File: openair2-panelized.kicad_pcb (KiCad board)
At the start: 2 copper layers, 175 x 96 mm, 423 parts, among them IC2 FT231XQ, IC3 SC189Z, IC5 SI7006-A20, IC6 RFM95W, P1 PM, P2 MOD1, P3 MOD2, P4 FAN, P5 PWR, T2 MMBT2222ALT3G, T3 MMBT2222ALT3G, U1 MIC2004-1.2YM5

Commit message: added link to proper tag
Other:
- board text added: "https://github.com/OpenAirCgn/openairnode-hw/tree/cgn-noise-i2s"
- board text removed: "https://github.com/OpenAirCgn/openairnode-hw"
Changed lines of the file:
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@@
     (effects (font (size 3 3) (thickness 0.6)) (justify left))
   )
-  (gr_text https://github.com/OpenAirCgn/openairnode-hw (at 47.1 127.9) (layer F.Cu)
-    (effects (font (size 3 3) (thickness 0.6)) (justify left))
+  (gr_text https://github.com/OpenAirCgn/openairnode-hw/tree/cgn-noise-i2s (at 47.1 127.9) (layer F.Cu)
+    (effects (font (size 1.5 1.5) (thickness 0.3)) (justify left))
   )
   (gr_text JLCJLCJLCJLC (at 206.9 55.2 90) (layer F.Cu)

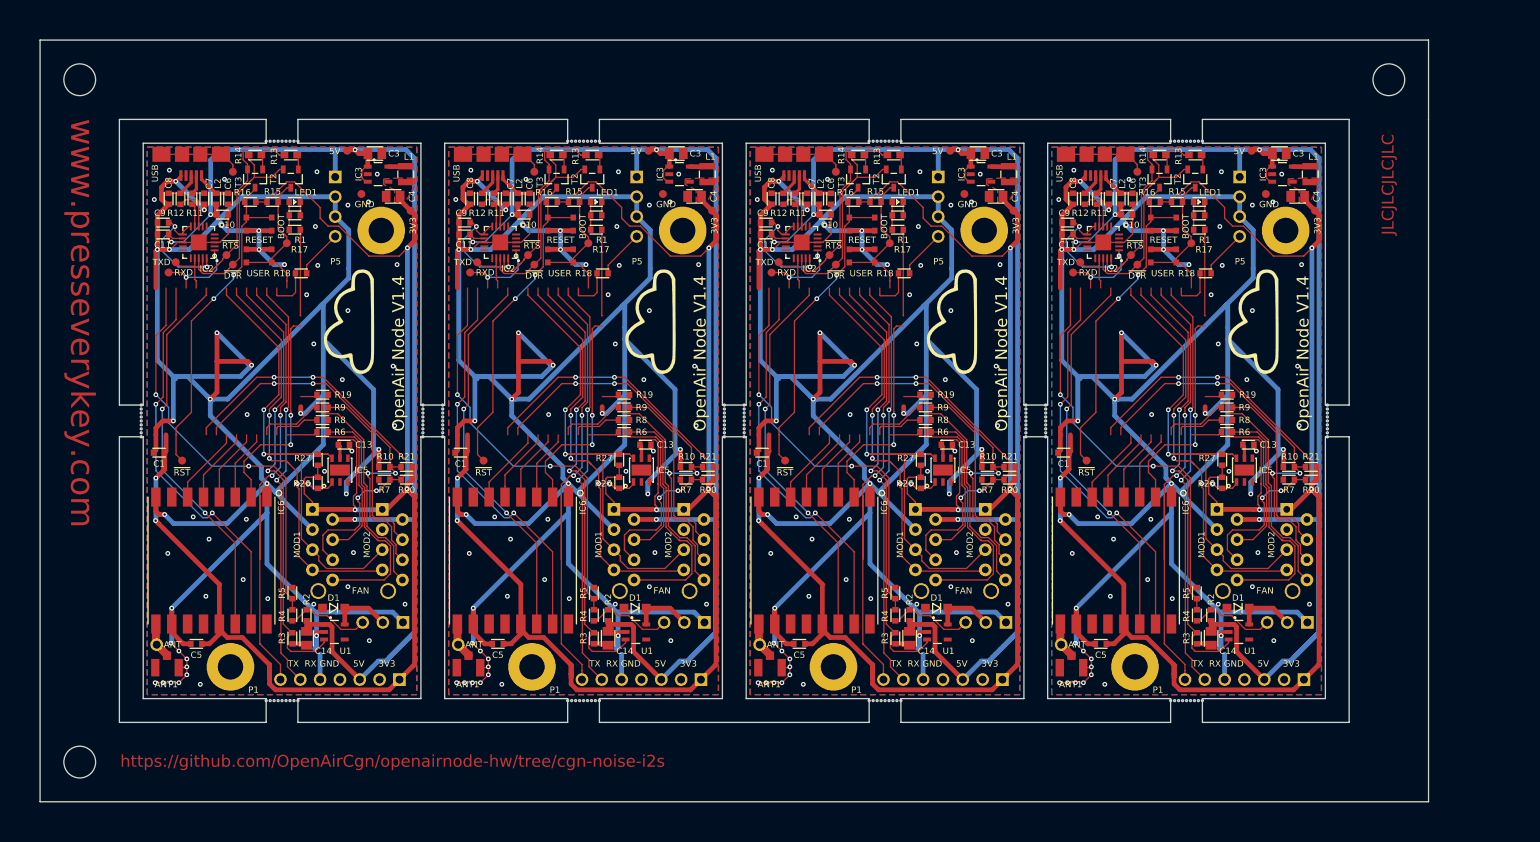
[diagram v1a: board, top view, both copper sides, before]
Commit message: more room for antenna overhang
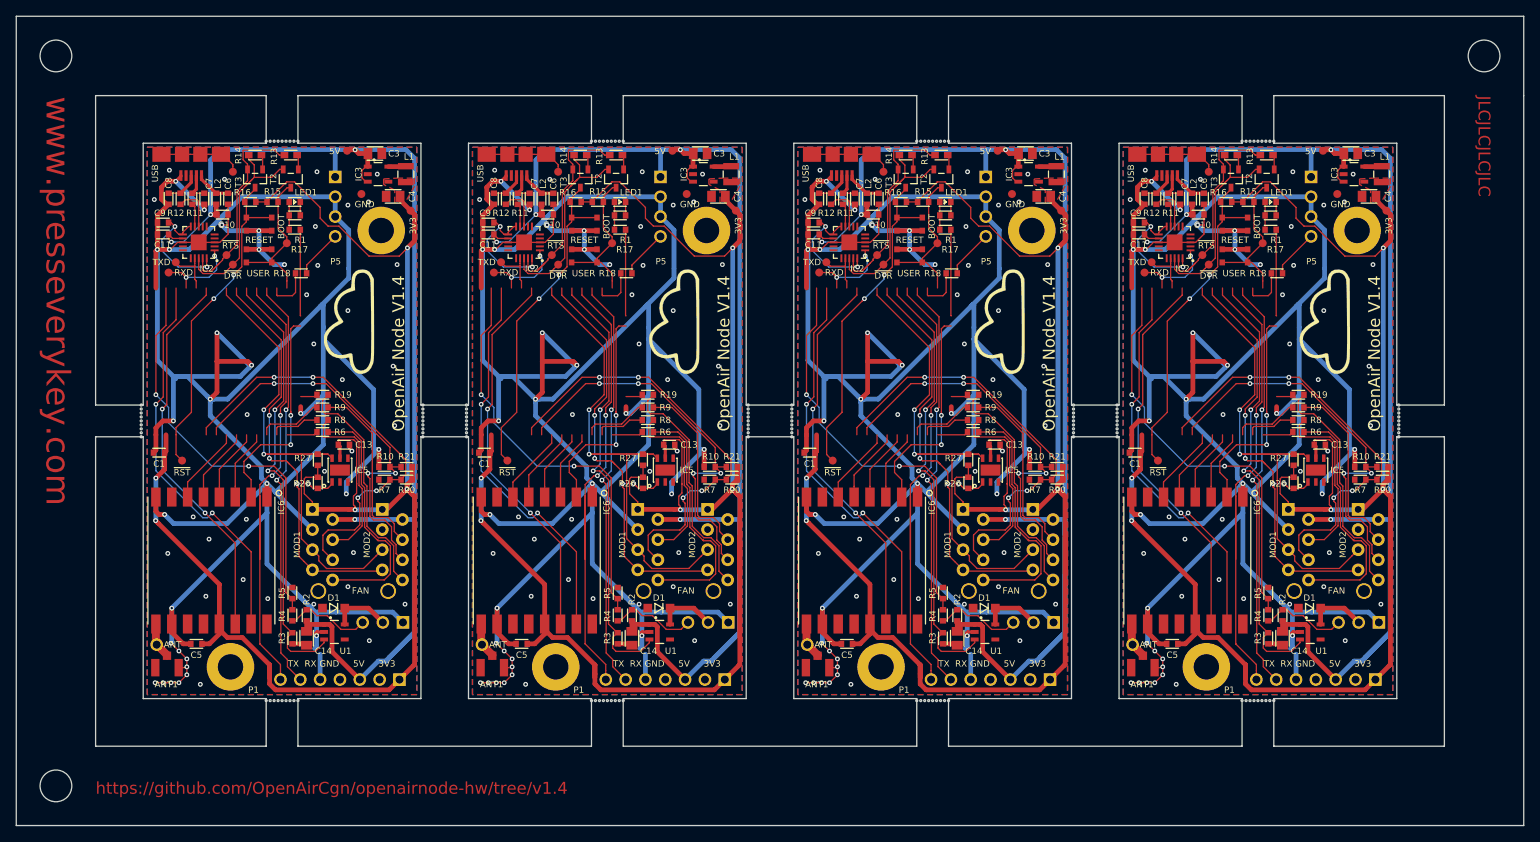
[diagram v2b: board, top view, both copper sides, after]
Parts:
- removed the ANT1 at (167.0, 116.1)
- removed the ANT1 at (129.0, 116.1)
- removed the ANT1 at (91.0, 116.1)
- removed the BTN1 at (178.6, 60.2)
- removed the BTN1 at (140.6, 60.2)
- removed the BTN1 at (102.6, 60.2)
- removed the C1 at (166.0, 89.0)
- removed the C1 at (128.0, 89.0)
- removed the C1 at (90.0, 89.0)
- removed the C10 at (174.0, 59.0)
- removed the C10 at (136.0, 59.0)
- removed the C10 at (98.0, 59.0)
- removed the C11 at (166.5, 61.5)
- removed the C11 at (128.5, 61.5)
- removed the C11 at (90.5, 61.5)
- removed the C13 at (189.3, 88.0)
- removed the C13 at (151.3, 88.0)
- removed the C13 at (113.3, 88.0)
- removed the C13 at (75.3, 88.0)
- removed the C14 at (184.6, 112.4)
- removed the C14 at (146.6, 112.4)
- removed the C14 at (108.6, 112.4)
- removed the C3 at (193.2, 51.3)
- removed the C3 at (155.2, 51.3)
- removed the C3 at (117.2, 51.3)
- removed the C4 at (195.5, 56.7)
- removed the C4 at (157.5, 56.7)
- removed the C4 at (119.5, 56.7)
- removed the C5 at (170.7, 113.1)
- removed the C5 at (132.7, 113.1)
- removed the C5 at (94.7, 113.1)
- removed the C5 at (56.7, 113.1)
- removed the C6 at (174.7, 57.0)
- removed the C6 at (136.7, 57.0)
- removed the C6 at (98.7, 57.0)
- removed the C7 at (171.7, 57.0)
- removed the C7 at (133.7, 57.0)
- removed the C7 at (95.7, 57.0)
- removed the C8 at (167.2, 57.0)
- removed the C8 at (129.2, 57.0)
- removed the C8 at (91.2, 57.0)
- removed the C9 at (166.5, 60.0)
- removed the C9 at (128.5, 60.0)
- removed the C9 at (90.5, 60.0)
- removed the C9 at (52.5, 60.0)
- removed the D1 at (188.0, 108.6)
- removed the D1 at (150.0, 108.6)
- removed the D1 at (112.0, 108.6)
- removed the H1 at (175.0, 116.0)
- removed the H1 at (137.0, 116.0)
- removed the H1 at (99.0, 116.0)
- removed the H2 at (194.0, 61.0)
- removed the H2 at (156.0, 61.0)
- removed the H2 at (118.0, 61.0)
- removed the IC2 at (171.0, 62.5)
- removed the IC2 at (133.0, 62.5)
- removed the IC2 at (95.0, 62.5)
- removed the IC2 at (57.0, 62.5)
- removed the IC3 at (193.6, 53.9)
- removed the IC3 at (155.6, 53.9)
- removed the IC3 at (117.6, 53.9)
- removed the IC5 at (188.8, 91.2)
- removed the IC5 at (150.8, 91.2)
- removed the IC5 at (112.8, 91.2)
- removed the IC6 at (172.6, 102.6)
- removed the IC6 at (134.6, 102.6)
- removed the IC6 at (96.6, 102.6)
- removed the L1 at (197.1, 53.9)
- removed the L1 at (159.1, 53.9)
- removed the L1 at (121.1, 53.9)
- removed the L2 at (173.2, 57.0)
- removed the L2 at (135.2, 57.0)
- removed the L2 at (97.2, 57.0)
- removed the LED1 at (183.1, 57.4)
- removed the LED1 at (145.1, 57.4)
- removed the LED1 at (107.1, 57.4)
- removed the LOGO1 at (189.9, 72.5)
- removed the LOGO1 at (151.9, 72.5)
- removed the LOGO1 at (113.9, 72.5)
- removed the P1 at (188.8, 117.6)
- removed the P1 at (150.8, 117.6)
- removed the P1 at (112.8, 117.6)
- removed the P2 at (186.6, 100.6)
- removed the P2 at (148.6, 100.6)
- removed the P2 at (110.6, 100.6)
- removed the P3 at (195.4, 100.6)
- removed the P3 at (157.4, 100.6)
- removed the P3 at (119.4, 100.6)
- removed the P4 at (194.2, 110.4)
- removed the P4 at (156.2, 110.4)
- removed the P4 at (118.2, 110.4)
- removed the P4 at (80.2, 110.4)
- removed the P5 at (188.2, 58.0)
- removed the P5 at (150.2, 58.0)
- removed the P5 at (112.2, 58.0)
- removed the R1 at (183.1, 59.1)
- removed the R1 at (145.1, 59.1)
- removed the R1 at (107.1, 59.1)
- removed the R10 at (194.4, 90.8)
- removed the R10 at (156.4, 90.8)
- removed the R10 at (118.4, 90.8)
- removed the R10 at (80.4, 90.8)
- removed the R11 at (170.2, 57.0)
- removed the R11 at (132.2, 57.0)
- removed the R11 at (94.2, 57.0)
- removed the R13 at (182.6, 51.5)
- removed the R13 at (144.6, 51.5)
- removed the R13 at (106.6, 51.5)
- removed the R15 at (180.3, 57.4)
- removed the R15 at (142.3, 57.4)
- removed the R15 at (104.3, 57.4)
- removed the R16 at (177.5, 57.4)
- removed the R16 at (139.5, 57.4)
- removed the R16 at (101.5, 57.4)
- removed the R17 at (183.1, 60.9)
- removed the R17 at (145.1, 60.9)
- removed the R17 at (107.1, 60.9)
- removed the R18 at (183.9, 66.4)
- removed the R18 at (145.9, 66.4)
- removed the R18 at (107.9, 66.4)
- removed the R19 at (186.6, 81.7)
- removed the R19 at (148.6, 81.7)
- removed the R19 at (110.6, 81.7)
- removed the R2 at (184.6, 109.5)
- removed the R2 at (146.6, 109.5)
- removed the R2 at (108.6, 109.5)
- removed the R20 at (197.2, 92.4)
- removed the R20 at (159.2, 92.4)
- removed the R20 at (121.2, 92.4)
- removed the R21 at (197.2, 90.8)
- removed the R21 at (159.2, 90.8)
- removed the R21 at (121.2, 90.8)
- removed the R26 at (186.0, 92.8)
- removed the R26 at (148.0, 92.8)
- removed the R26 at (110.0, 92.8)
- removed the R27 at (186.0, 89.9)
- removed the R27 at (148.0, 89.9)
- removed the R27 at (110.0, 89.9)
- removed the R4 at (182.8, 109.5)
- removed the R4 at (144.8, 109.5)
- removed the R4 at (106.8, 109.5)
- removed the R5 at (182.8, 106.7)
- removed the R5 at (144.8, 106.7)
- removed the R5 at (106.8, 106.7)
- removed the R6 at (186.6, 86.4)
- removed the R6 at (148.6, 86.4)
- removed the R6 at (110.6, 86.4)
- removed the R7 at (194.4, 92.4)
- removed the R7 at (156.4, 92.4)
- removed the R7 at (118.4, 92.4)
- removed the R8 at (186.6, 84.9)
- removed the R8 at (148.6, 84.9)
- removed the R8 at (110.6, 84.9)
- removed the R9 at (186.6, 83.3)
- removed the R9 at (148.6, 83.3)
- removed the R9 at (110.6, 83.3)
- removed the REF** at (199.3, 83.0)
- removed the REF** at (163.7, 87.0)
- removed the REF** at (141.5, 49.7)
- removed the REF** at (142.0, 49.7)
- removed the REF** at (142.5, 49.7)
- removed the REF** at (143.0, 49.7)
- removed the REF** at (143.5, 49.7)
- removed the REF** at (144.0, 49.7)
- removed the REF** at (144.5, 49.7)
- removed the REF** at (145.0, 49.7)
- removed the REF** at (145.5, 49.7)
- removed the REF** at (163.7, 86.5)
- removed the REF** at (106.0, 120.3)
- removed the REF** at (105.5, 120.3)
- removed the REF** at (105.0, 120.3)
- removed the REF** at (104.5, 120.3)
- removed the REF** at (104.0, 120.3)
- removed the REF** at (103.5, 120.3)
- removed the REF** at (103.5, 49.7)
- removed the REF** at (104.0, 49.7)
- removed the REF** at (163.7, 86.0)
- removed the REF** at (104.5, 49.7)
- removed the REF** at (105.0, 49.7)
- removed the REF** at (105.5, 49.7)
- removed the REF** at (106.0, 49.7)
- removed the REF** at (163.7, 85.5)
- removed the REF** at (163.7, 85.0)
- removed the REF** at (42.0, 128.0)
- removed the REF** at (207.0, 42.0)
- removed the REF** at (42.0, 42.0)
- removed the REF** at (163.7, 84.5)
- removed the REF** at (163.7, 84.0)
- removed the REF** at (163.7, 83.5)
- removed the REF** at (163.7, 83.0)
- removed the REF** at (161.3, 83.0)
- removed the REF** at (199.3, 83.5)
- removed the REF** at (161.3, 83.5)
- removed the REF** at (161.3, 84.0)
- removed the REF** at (161.3, 84.5)
- removed the REF** at (161.3, 85.0)
- removed the REF** at (161.3, 85.5)
- removed the REF** at (161.3, 86.0)
- removed the REF** at (161.3, 86.5)
- removed the REF** at (161.3, 87.0)
- removed the REF** at (125.7, 87.0)
- removed the REF** at (125.7, 86.5)
- removed the REF** at (199.3, 84.0)
- removed the REF** at (125.7, 85.5)
- removed the REF** at (125.7, 85.0)
- removed the REF** at (125.7, 84.5)
- removed the REF** at (125.7, 84.0)
- removed the REF** at (125.7, 83.5)
- removed the REF** at (125.7, 83.0)
- removed the REF** at (123.3, 83.0)
- removed the REF** at (123.3, 83.5)
- removed the REF** at (123.3, 84.0)
- removed the REF** at (199.3, 84.5)
- removed the REF** at (123.3, 85.0)
- removed the REF** at (123.3, 85.5)
- removed the REF** at (123.3, 86.0)
- removed the REF** at (123.3, 86.5)
- removed the REF** at (123.3, 87.0)
- removed the REF** at (87.7, 87.0)
- removed the REF** at (87.7, 86.5)
- removed the REF** at (87.7, 86.0)
- removed the REF** at (87.7, 85.5)
- removed the REF** at (87.7, 84.5)
- removed the REF** at (87.7, 84.0)
- removed the REF** at (87.7, 83.5)
- removed the REF** at (87.7, 83.0)
- removed the REF** at (199.3, 85.5)
- removed the REF** at (199.3, 86.0)
- removed the REF** at (183.5, 120.3)
- removed the REF** at (183.0, 120.3)
- removed the REF** at (182.5, 120.3)
- removed the REF** at (182.0, 120.3)
- removed the REF** at (181.5, 120.3)
- removed the REF** at (180.5, 120.3)
- removed the REF** at (199.3, 86.5)
- removed the REF** at (180.0, 120.3)
- removed the REF** at (179.5, 120.3)
- removed the REF** at (179.5, 49.7)
- removed the REF** at (180.0, 49.7)
- removed the REF** at (180.5, 49.7)
- removed the REF** at (181.0, 49.7)
- removed the REF** at (181.5, 49.7)
- removed the REF** at (182.0, 49.7)
- removed the REF** at (182.5, 49.7)
- removed the REF** at (183.0, 49.7)
- removed the REF** at (199.3, 87.0)
- removed the REF** at (183.5, 49.7)
- removed the REF** at (145.5, 120.3)
- removed the REF** at (145.0, 120.3)
- removed the REF** at (144.5, 120.3)
- removed the REF** at (144.0, 120.3)
- removed the REF** at (143.5, 120.3)
- removed the REF** at (143.0, 120.3)
- removed the REF** at (142.5, 120.3)
- removed the REF** at (142.0, 120.3)
- removed the REF** at (141.5, 120.3)
- removed the T2 at (182.6, 54.5)
- removed the T2 at (144.6, 54.5)
- removed the T2 at (106.6, 54.5)
- removed the T3 at (178.1, 54.5)
- removed the T3 at (140.1, 54.5)
- removed the T3 at (102.1, 54.5)
- removed the TP1 at (189.7, 51.0)
- removed the TP1 at (151.7, 51.0)
- removed the TP1 at (113.7, 51.0)
- removed the TP10 at (168.9, 90.0)
- removed the TP10 at (130.9, 90.0)
- removed the TP10 at (92.9, 90.0)
- removed the TP11 at (182.1, 62.6)
- removed the TP11 at (144.1, 62.6)
- removed the TP11 at (106.1, 62.6)
- removed the TP2 at (197.7, 58.5)
- removed the TP2 at (159.7, 58.5)
- removed the TP2 at (121.7, 58.5)
- removed the TP3 at (191.5, 56.4)
- removed the TP3 at (153.5, 56.4)
- removed the TP3 at (115.5, 56.4)
- removed the TP4 at (168.1, 65.0)
- removed the TP4 at (130.1, 65.0)
- removed the TP4 at (92.1, 65.0)
- removed the TP5 at (174.5, 64.1)
- removed the TP5 at (136.5, 64.1)
- removed the TP5 at (98.5, 64.1)
- removed the TP6 at (167.2, 66.3)
- removed the TP6 at (129.2, 66.3)
- removed the TP6 at (91.2, 66.3)
- removed the TP8 at (175.3, 53.6)
- removed the TP8 at (137.3, 53.6)
- removed the TP8 at (99.3, 53.6)
- removed the TP9 at (165.7, 113.2)
- removed the TP9 at (127.7, 113.2)
- removed the TP9 at (89.7, 113.2)
- removed the U1 at (188.1, 111.6)
- removed the U1 at (150.1, 111.6)
- removed the U1 at (112.1, 111.6)
- added ANT1: CONN_2, everykey:U-FL, F.Cu at (176.0, 116.1)
- added ANT1: CONN_2, everykey:U-FL, F.Cu at (135.0, 116.1)
- added ANT1: CONN_2, everykey:U-FL, F.Cu at (94.0, 116.1)
- added BTN1: RESET, everykey:CK-PTS830, F.Cu at (187.6, 60.2)
- added BTN1: RESET, everykey:CK-PTS830, F.Cu at (146.6, 60.2)
- added BTN1: RESET, everykey:CK-PTS830, F.Cu at (105.6, 60.2)
- added BTN2: USER, everykey:CK-PTS830, F.Cu at (187.6, 64.2)
- added BTN2: USER, everykey:CK-PTS830, F.Cu at (146.6, 64.2)
- added BTN2: USER, everykey:CK-PTS830, F.Cu at (105.6, 64.2)
- added C1: 0.1u, everykey:0603, F.Cu at (175.0, 89.0)
- added C1: 0.1u, everykey:0603, F.Cu at (134.0, 89.0)
- added C1: 0.1u, everykey:0603, F.Cu at (93.0, 89.0)
- added C10: 4u7, everykey:0603, F.Cu at (183.0, 59.0)
- added C10: 4u7, everykey:0603, F.Cu at (142.0, 59.0)
- added C10: 4u7, everykey:0603, F.Cu at (101.0, 59.0)
- added C11: 0u1, everykey:0603, F.Cu at (175.5, 61.5)
- added C11: 0u1, everykey:0603, F.Cu at (134.5, 61.5)
- added C11: 0u1, everykey:0603, F.Cu at (93.5, 61.5)
- added C13: 0u1, everykey:0603, F.Cu at (198.3, 88.0)
- added C14: 10u, everykey:0805, F.Cu at (193.6, 112.4)
- added C14: 10u, everykey:0805, F.Cu at (152.6, 112.4)
- added C14: 10u, everykey:0805, F.Cu at (111.6, 112.4)
- added C3: 10u, everykey:0805, F.Cu at (202.2, 51.3)
- added C3: 10u, everykey:0805, F.Cu at (161.2, 51.3)
- added C3: 10u, everykey:0805, F.Cu at (120.2, 51.3)
- added C4: 10u, everykey:0805, F.Cu at (204.5, 56.7)
- added C4: 10u, everykey:0805, F.Cu at (163.5, 56.7)
- added C4: 10u, everykey:0805, F.Cu at (122.5, 56.7)
- added C5: 0.1u, everykey:0603, F.Cu at (179.7, 113.1)
- added C6: 10n, everykey:0603, F.Cu at (183.7, 57.0)
- added C6: 10n, everykey:0603, F.Cu at (142.7, 57.0)
- added C6: 10n, everykey:0603, F.Cu at (101.7, 57.0)
- added C7: 47p, everykey:0603, F.Cu at (139.7, 57.0)
- added C7: 47p, everykey:0603, F.Cu at (98.7, 57.0)
- added C8: 47p, everykey:0603, F.Cu at (176.2, 57.0)
- added C8: 47p, everykey:0603, F.Cu at (135.2, 57.0)
- added C8: 47p, everykey:0603, F.Cu at (94.2, 57.0)
- added C9: 0u1, everykey:0603, F.Cu at (175.5, 60.0)
- added D1: D_Schottky, everykey:SOD-123F, F.Cu at (197.0, 108.6)
- added D1: D_Schottky, everykey:SOD-123F, F.Cu at (156.0, 108.6)
- added D1: D_Schottky, everykey:SOD-123F, F.Cu at (115.0, 108.6)
- added H1: HOLE, everykey:HOLE-3.2, F.Cu at (184.0, 116.0)
- added H1: HOLE, everykey:HOLE-3.2, F.Cu at (143.0, 116.0)
- added H1: HOLE, everykey:HOLE-3.2, F.Cu at (102.0, 116.0)
- added H2: HOLE, everykey:HOLE-3.2, F.Cu at (203.0, 61.0)
- added H2: HOLE, everykey:HOLE-3.2, F.Cu at (162.0, 61.0)
- added H2: HOLE, everykey:HOLE-3.2, F.Cu at (121.0, 61.0)
- added IC2: FT231XQ, everykey:QFN-20, F.Cu at (180.0, 62.5)
- added IC3: SC189Z, everykey:SOT23-5, F.Cu at (202.6, 53.9)
- added IC3: SC189Z, everykey:SOT23-5, F.Cu at (161.6, 53.9)
- added IC3: SC189Z, everykey:SOT23-5, F.Cu at (120.6, 53.9)
- added IC5: SI7006-A20, everykey:SI7006-A20, F.Cu at (197.8, 91.2)
- added IC5: SI7006-A20, everykey:SI7006-A20, F.Cu at (156.8, 91.2)
- added IC5: SI7006-A20, everykey:SI7006-A20, F.Cu at (115.8, 91.2)
- added IC6: RFM95W, everykey:RFM95W-SMD, F.Cu at (181.6, 102.6)
- added IC6: RFM95W, everykey:RFM95W-SMD, F.Cu at (140.6, 102.6)
- added IC6: RFM95W, everykey:RFM95W-SMD, F.Cu at (99.6, 102.6)
- added L1: 2.2u 1A BDCD002520122R2MS1, everykey:1008-2520, F.Cu at (206.1, 53.9)
- added L1: 2.2u 1A BDCD002520122R2MS1, everykey:1008-2520, F.Cu at (165.1, 53.9)
- added L1: 2.2u 1A BDCD002520122R2MS1, everykey:1008-2520, F.Cu at (124.1, 53.9)
- added L2: FERRITE, everykey:0603, F.Cu at (182.2, 57.0)
- added L2: FERRITE, everykey:0603, F.Cu at (141.2, 57.0)
- added L2: FERRITE, everykey:0603, F.Cu at (100.2, 57.0)
- added LED1: LED, everykey:0603-POLAR, F.Cu at (192.1, 57.4)
- added LED1: LED, everykey:0603-POLAR, F.Cu at (151.1, 57.4)
- added LED1: LED, everykey:0603-POLAR, F.Cu at (110.1, 57.4)
- added LOGO1: Logo, Logo:Logo, F.Cu at (198.9, 72.5)
- added LOGO1: Logo, Logo:Logo, F.Cu at (157.9, 72.5)
- added LOGO1: Logo, Logo:Logo, F.Cu at (116.9, 72.5)
- added P1: PM, everykey:HEADER-1x07-2.5-JST-XH, F.Cu at (197.8, 117.6)
- added P1: PM, everykey:HEADER-1x07-2.5-JST-XH, F.Cu at (156.8, 117.6)
- added P1: PM, everykey:HEADER-1x07-2.5-JST-XH, F.Cu at (115.8, 117.6)
- added P2: MOD1, everykey:HEADER-1x08-1.27-ZZ-POL, F.Cu at (195.6, 100.6)
- added P2: MOD1, everykey:HEADER-1x08-1.27-ZZ-POL, F.Cu at (154.6, 100.6)
- added P2: MOD1, everykey:HEADER-1x08-1.27-ZZ-POL, F.Cu at (113.6, 100.6)
- added P3: MOD2, everykey:HEADER-1x08-1.27-ZZ-POL, F.Cu at (204.4, 100.6)
- added P3: MOD2, everykey:HEADER-1x08-1.27-ZZ-POL, F.Cu at (163.4, 100.6)
- added P3: MOD2, everykey:HEADER-1x08-1.27-ZZ-POL, F.Cu at (122.4, 100.6)
- added P4: FAN, everykey:HEADER-1x03-2.54, F.Cu at (203.2, 110.4)
- added P5: PWR, everykey:HEADER-1x04-2.5-JST-XH, F.Cu at (156.2, 58.0)
- added P5: PWR, everykey:HEADER-1x04-2.5-JST-XH, F.Cu at (115.2, 58.0)
- added R1: 10K, everykey:0603, F.Cu at (192.1, 59.1)
- added R1: 10K, everykey:0603, F.Cu at (151.1, 59.1)
- added R1: 10K, everykey:0603, F.Cu at (110.1, 59.1)
- added R10: 47K, everykey:0603, F.Cu at (203.4, 90.8)
- added R11: 27, everykey:0603, F.Cu at (138.2, 57.0)
- added R11: 27, everykey:0603, F.Cu at (97.2, 57.0)
- added R12: 27, everykey:0603, F.Cu at (177.7, 57.0)
- added R12: 27, everykey:0603, F.Cu at (136.7, 57.0)
- added R12: 27, everykey:0603, F.Cu at (95.7, 57.0)
- added R13: 10K, everykey:0603, F.Cu at (191.6, 51.5)
- added R13: 10K, everykey:0603, F.Cu at (150.6, 51.5)
- added R13: 10K, everykey:0603, F.Cu at (109.6, 51.5)
- added R14: 10K, everykey:0603, F.Cu at (187.1, 51.5)
- added R14: 10K, everykey:0603, F.Cu at (146.1, 51.5)
- added R14: 10K, everykey:0603, F.Cu at (105.1, 51.5)
- added R15: 10K, everykey:0603, F.Cu at (189.3, 57.4)
- added R15: 10K, everykey:0603, F.Cu at (148.3, 57.4)
- added R15: 10K, everykey:0603, F.Cu at (107.3, 57.4)
- added R16: 10K, everykey:0603, F.Cu at (186.5, 57.4)
- added R16: 10K, everykey:0603, F.Cu at (145.5, 57.4)
- added R16: 10K, everykey:0603, F.Cu at (104.5, 57.4)
- added R17: 220, everykey:0603, F.Cu at (151.1, 60.9)
- added R17: 220, everykey:0603, F.Cu at (110.1, 60.9)
- added R18: 220, everykey:0603, F.Cu at (192.9, 66.4)
- added R18: 220, everykey:0603, F.Cu at (151.9, 66.4)
- added R18: 220, everykey:0603, F.Cu at (110.9, 66.4)
- added R19: 27, everykey:0603, F.Cu at (195.6, 81.7)
- added R19: 27, everykey:0603, F.Cu at (154.6, 81.7)
- added R19: 27, everykey:0603, F.Cu at (113.6, 81.7)
- added R2: 1K, everykey:0603, F.Cu at (152.6, 109.5)
- added R2: 1K, everykey:0603, F.Cu at (111.6, 109.5)
- added R20: DNP, everykey:0603, F.Cu at (206.2, 92.4)
- added R20: DNP, everykey:0603, F.Cu at (165.2, 92.4)
- added R20: DNP, everykey:0603, F.Cu at (124.2, 92.4)
- added R21: DNP, everykey:0603, F.Cu at (206.2, 90.8)
- added R21: DNP, everykey:0603, F.Cu at (165.2, 90.8)
- added R21: DNP, everykey:0603, F.Cu at (124.2, 90.8)
- added R26: 2K2, everykey:0603, F.Cu at (195.0, 92.8)
- added R26: 2K2, everykey:0603, F.Cu at (154.0, 92.8)
- added R26: 2K2, everykey:0603, F.Cu at (113.0, 92.8)
- added R27: 2K2, everykey:0603, F.Cu at (195.0, 89.9)
- added R27: 2K2, everykey:0603, F.Cu at (154.0, 89.9)
- added R27: 2K2, everykey:0603, F.Cu at (113.0, 89.9)
- added R3: 10K, everykey:0603, F.Cu at (191.8, 112.4)
- added R3: 10K, everykey:0603, F.Cu at (150.8, 112.4)
- added R3: 10K, everykey:0603, F.Cu at (109.8, 112.4)
- added R4: 10K, everykey:0603, F.Cu at (191.8, 109.5)
- added R4: 10K, everykey:0603, F.Cu at (150.8, 109.5)
- added R4: 10K, everykey:0603, F.Cu at (109.8, 109.5)
- added R5: 22K, everykey:0603, F.Cu at (191.8, 106.7)
- added R5: 22K, everykey:0603, F.Cu at (150.8, 106.7)
- added R5: 22K, everykey:0603, F.Cu at (109.8, 106.7)
- added R6: 27, everykey:0603, F.Cu at (195.6, 86.4)
- added R6: 27, everykey:0603, F.Cu at (154.6, 86.4)
- added R6: 27, everykey:0603, F.Cu at (113.6, 86.4)
- added R7: 47K, everykey:0603, F.Cu at (203.4, 92.4)
- added R7: 47K, everykey:0603, F.Cu at (162.4, 92.4)
- added R7: 47K, everykey:0603, F.Cu at (121.4, 92.4)
- added R8: 27, everykey:0603, F.Cu at (154.6, 84.9)
- added R8: 27, everykey:0603, F.Cu at (113.6, 84.9)
- added R9: 27, everykey:0603, F.Cu at (195.6, 83.3)
- added R9: 27, everykey:0603, F.Cu at (154.6, 83.3)
- added R9: 27, everykey:0603, F.Cu at (113.6, 83.3)
- added REF**: NPTH, NPTH, F.Cu at (208.3, 83.0)
- added REF**: NPTH, NPTH, F.Cu at (172.7, 87.0)
- added REF**: NPTH, NPTH, F.Cu at (147.5, 49.7)
- added REF**: NPTH, NPTH, F.Cu at (148.0, 49.7)
- added REF**: NPTH, NPTH, F.Cu at (148.5, 49.7)
- added REF**: NPTH, NPTH, F.Cu at (149.0, 49.7)
- added REF**: NPTH, NPTH, F.Cu at (149.5, 49.7)
- added REF**: NPTH, NPTH, F.Cu at (150.0, 49.7)
- added REF**: NPTH, NPTH, F.Cu at (150.5, 49.7)
- added REF**: NPTH, NPTH, F.Cu at (151.0, 49.7)
- added REF**: NPTH, NPTH, F.Cu at (151.5, 49.7)
- added REF**: NPTH, NPTH, F.Cu at (110.5, 120.3)
- added REF**: NPTH, NPTH, F.Cu at (172.7, 86.5)
- added REF**: NPTH, NPTH, F.Cu at (110.0, 120.3)
- added REF**: NPTH, NPTH, F.Cu at (109.5, 120.3)
- added REF**: NPTH, NPTH, F.Cu at (109.0, 120.3)
- added REF**: NPTH, NPTH, F.Cu at (108.5, 120.3)
- added REF**: NPTH, NPTH, F.Cu at (108.0, 120.3)
- added REF**: NPTH, NPTH, F.Cu at (172.7, 86.0)
- added REF**: NPTH, NPTH, F.Cu at (108.0, 49.7)
- added REF**: NPTH, NPTH, F.Cu at (108.5, 49.7)
- added REF**: NPTH, NPTH, F.Cu at (109.0, 49.7)
- added REF**: NPTH, NPTH, F.Cu at (109.5, 49.7)
- added REF**: NPTH, NPTH, F.Cu at (110.0, 49.7)
- added REF**: NPTH, NPTH, F.Cu at (110.5, 49.7)
- added REF**: NPTH, NPTH, F.Cu at (172.7, 85.5)
- added REF**: NPTH, NPTH, F.Cu at (172.7, 85.0)
- added REF**: NPTH, NPTH, F.Cu at (39.0, 131.0)
- added REF**: NPTH, NPTH, F.Cu at (219.0, 39.0)
- added REF**: NPTH, NPTH, F.Cu at (39.0, 39.0)
- added REF**: NPTH, NPTH, F.Cu at (172.7, 84.5)
- added REF**: NPTH, NPTH, F.Cu at (172.7, 84.0)
- added REF**: NPTH, NPTH, F.Cu at (172.7, 83.5)
- added REF**: NPTH, NPTH, F.Cu at (172.7, 83.0)
- added REF**: NPTH, NPTH, F.Cu at (167.3, 83.0)
- added REF**: NPTH, NPTH, F.Cu at (208.3, 83.5)
- added REF**: NPTH, NPTH, F.Cu at (167.3, 83.5)
- added REF**: NPTH, NPTH, F.Cu at (167.3, 84.0)
- added REF**: NPTH, NPTH, F.Cu at (167.3, 84.5)
- added REF**: NPTH, NPTH, F.Cu at (167.3, 85.0)
- added REF**: NPTH, NPTH, F.Cu at (167.3, 85.5)
- added REF**: NPTH, NPTH, F.Cu at (167.3, 86.0)
- added REF**: NPTH, NPTH, F.Cu at (167.3, 86.5)
- added REF**: NPTH, NPTH, F.Cu at (167.3, 87.0)
- added REF**: NPTH, NPTH, F.Cu at (131.7, 87.0)
- added REF**: NPTH, NPTH, F.Cu at (131.7, 86.5)
- added REF**: NPTH, NPTH, F.Cu at (208.3, 84.0)
- added REF**: NPTH, NPTH, F.Cu at (131.7, 86.0)
- added REF**: NPTH, NPTH, F.Cu at (131.7, 85.5)
- added REF**: NPTH, NPTH, F.Cu at (131.7, 85.0)
- added REF**: NPTH, NPTH, F.Cu at (131.7, 84.5)
- added REF**: NPTH, NPTH, F.Cu at (131.7, 84.0)
- added REF**: NPTH, NPTH, F.Cu at (131.7, 83.5)
- added REF**: NPTH, NPTH, F.Cu at (131.7, 83.0)
- added REF**: NPTH, NPTH, F.Cu at (126.3, 83.0)
- added REF**: NPTH, NPTH, F.Cu at (126.3, 83.5)
- added REF**: NPTH, NPTH, F.Cu at (126.3, 84.0)
- added REF**: NPTH, NPTH, F.Cu at (208.3, 84.5)
- added REF**: NPTH, NPTH, F.Cu at (126.3, 84.5)
- added REF**: NPTH, NPTH, F.Cu at (126.3, 85.0)
- added REF**: NPTH, NPTH, F.Cu at (126.3, 85.5)
- added REF**: NPTH, NPTH, F.Cu at (126.3, 86.0)
- added REF**: NPTH, NPTH, F.Cu at (126.3, 86.5)
- added REF**: NPTH, NPTH, F.Cu at (126.3, 87.0)
- added REF**: NPTH, NPTH, F.Cu at (90.7, 87.0)
- added REF**: NPTH, NPTH, F.Cu at (90.7, 86.5)
- added REF**: NPTH, NPTH, F.Cu at (90.7, 86.0)
- added REF**: NPTH, NPTH, F.Cu at (90.7, 85.5)
- added REF**: NPTH, NPTH, F.Cu at (208.3, 85.0)
- added REF**: NPTH, NPTH, F.Cu at (90.7, 85.0)
- added REF**: NPTH, NPTH, F.Cu at (90.7, 84.5)
- added REF**: NPTH, NPTH, F.Cu at (90.7, 84.0)
- added REF**: NPTH, NPTH, F.Cu at (90.7, 83.5)
- added REF**: NPTH, NPTH, F.Cu at (90.7, 83.0)
- added REF**: NPTH, NPTH, F.Cu at (208.3, 85.5)
- added REF**: NPTH, NPTH, F.Cu at (49.7, 87.0)
- added REF**: NPTH, NPTH, F.Cu at (208.3, 86.0)
- added REF**: NPTH, NPTH, F.Cu at (192.5, 120.3)
- added REF**: NPTH, NPTH, F.Cu at (192.0, 120.3)
- added REF**: NPTH, NPTH, F.Cu at (191.5, 120.3)
- added REF**: NPTH, NPTH, F.Cu at (191.0, 120.3)
- added REF**: NPTH, NPTH, F.Cu at (190.5, 120.3)
- added REF**: NPTH, NPTH, F.Cu at (190.0, 120.3)
- added REF**: NPTH, NPTH, F.Cu at (189.5, 120.3)
- added REF**: NPTH, NPTH, F.Cu at (208.3, 86.5)
- added REF**: NPTH, NPTH, F.Cu at (189.0, 120.3)
- added REF**: NPTH, NPTH, F.Cu at (188.5, 120.3)
- added REF**: NPTH, NPTH, F.Cu at (188.5, 49.7)
- added REF**: NPTH, NPTH, F.Cu at (189.0, 49.7)
- added REF**: NPTH, NPTH, F.Cu at (189.5, 49.7)
- added REF**: NPTH, NPTH, F.Cu at (190.0, 49.7)
- added REF**: NPTH, NPTH, F.Cu at (190.5, 49.7)
- added REF**: NPTH, NPTH, F.Cu at (191.0, 49.7)
- added REF**: NPTH, NPTH, F.Cu at (191.5, 49.7)
- added REF**: NPTH, NPTH, F.Cu at (192.0, 49.7)
- added REF**: NPTH, NPTH, F.Cu at (208.3, 87.0)
- added REF**: NPTH, NPTH, F.Cu at (192.5, 49.7)
- added REF**: NPTH, NPTH, F.Cu at (151.5, 120.3)
- added REF**: NPTH, NPTH, F.Cu at (151.0, 120.3)
- added REF**: NPTH, NPTH, F.Cu at (150.5, 120.3)
- added REF**: NPTH, NPTH, F.Cu at (150.0, 120.3)
- added REF**: NPTH, NPTH, F.Cu at (149.5, 120.3)
- added REF**: NPTH, NPTH, F.Cu at (149.0, 120.3)
- added REF**: NPTH, NPTH, F.Cu at (148.5, 120.3)
- added REF**: NPTH, NPTH, F.Cu at (148.0, 120.3)
- added REF**: NPTH, NPTH, F.Cu at (147.5, 120.3)
- added T2: MMBT2222ALT3G, everykey:SOT23-3, F.Cu at (191.6, 54.5)
- added T2: MMBT2222ALT3G, everykey:SOT23-3, F.Cu at (150.6, 54.5)
- added T2: MMBT2222ALT3G, everykey:SOT23-3, F.Cu at (109.6, 54.5)
- added T3: MMBT2222ALT3G, everykey:SOT23-3, F.Cu at (187.1, 54.5)
- added T3: MMBT2222ALT3G, everykey:SOT23-3, F.Cu at (146.1, 54.5)
- added T3: MMBT2222ALT3G, everykey:SOT23-3, F.Cu at (105.1, 54.5)
- added TP1: 5V, everykey:TESTPOINT_1mm, F.Cu at (198.7, 51.0)
- added TP1: 5V, everykey:TESTPOINT_1mm, F.Cu at (157.7, 51.0)
- added TP1: 5V, everykey:TESTPOINT_1mm, F.Cu at (116.7, 51.0)
- added TP10: ~RST, everykey:TESTPOINT_1mm, F.Cu at (177.9, 90.0)
- added TP10: ~RST, everykey:TESTPOINT_1mm, F.Cu at (136.9, 90.0)
- added TP10: ~RST, everykey:TESTPOINT_1mm, F.Cu at (95.9, 90.0)
- added TP11: BOOT, everykey:TESTPOINT_1mm, F.Cu at (191.1, 62.6)
- added TP11: BOOT, everykey:TESTPOINT_1mm, F.Cu at (150.1, 62.6)
- added TP11: BOOT, everykey:TESTPOINT_1mm, F.Cu at (109.1, 62.6)
- added TP2: 3V3, everykey:TESTPOINT_1mm, F.Cu at (206.7, 58.5)
- added TP2: 3V3, everykey:TESTPOINT_1mm, F.Cu at (165.7, 58.5)
- added TP2: 3V3, everykey:TESTPOINT_1mm, F.Cu at (124.7, 58.5)
- added TP3: GND, everykey:TESTPOINT_1mm, F.Cu at (200.5, 56.4)
- added TP3: GND, everykey:TESTPOINT_1mm, F.Cu at (159.5, 56.4)
- added TP3: GND, everykey:TESTPOINT_1mm, F.Cu at (118.5, 56.4)
- added TP4: TXD, everykey:TESTPOINT_1mm, F.Cu at (177.1, 65.0)
- added TP4: TXD, everykey:TESTPOINT_1mm, F.Cu at (136.1, 65.0)
- added TP4: TXD, everykey:TESTPOINT_1mm, F.Cu at (95.1, 65.0)
- added TP5: ~RTS, everykey:TESTPOINT_1mm, F.Cu at (183.5, 64.1)
- added TP5: ~RTS, everykey:TESTPOINT_1mm, F.Cu at (142.5, 64.1)
- added TP5: ~RTS, everykey:TESTPOINT_1mm, F.Cu at (101.5, 64.1)
- added TP6: RXD, everykey:TESTPOINT_1mm, F.Cu at (176.2, 66.3)
- added TP6: RXD, everykey:TESTPOINT_1mm, F.Cu at (135.2, 66.3)
- added TP6: RXD, everykey:TESTPOINT_1mm, F.Cu at (94.2, 66.3)
- added TP7: ~DTR, everykey:TESTPOINT_1mm, F.Cu at (184.3, 65.3)
- added TP7: ~DTR, everykey:TESTPOINT_1mm, F.Cu at (143.3, 65.3)
- added TP7: ~DTR, everykey:TESTPOINT_1mm, F.Cu at (102.3, 65.3)
- added TP8: SHLD, everykey:TESTPOINT_1mm, F.Cu at (184.3, 53.6)
- added TP8: SHLD, everykey:TESTPOINT_1mm, F.Cu at (143.3, 53.6)
- added TP8: SHLD, everykey:TESTPOINT_1mm, F.Cu at (102.3, 53.6)
- added TP9: ANT, everykey:HEADER-1x01, F.Cu at (174.7, 113.2)
- added TP9: ANT, everykey:HEADER-1x01, F.Cu at (133.7, 113.2)
- added TP9: ANT, everykey:HEADER-1x01, F.Cu at (92.7, 113.2)
- added U1: MIC2004-1.2YM5, everykey:SOT23-5, F.Cu at (197.1, 111.6)
- added U1: MIC2004-1.2YM5, everykey:SOT23-5, F.Cu at (156.1, 111.6)
- added U1: MIC2004-1.2YM5, everykey:SOT23-5, F.Cu at (115.1, 111.6)
- added USB1: USB, everykey:USB-MICRO-B, F.Cu at (179.1, 51.4)
- added USB1: USB, everykey:USB-MICRO-B, F.Cu at (138.1, 51.4)
- added USB1: USB, everykey:USB-MICRO-B, F.Cu at (97.1, 51.4)
- C13 (x3): renamed from R12; value 27 -> 0u1
- C5 (x3): renamed from TP7; value ~DTR -> 0.1u; footprint everykey:TESTPOINT_1mm -> everykey:0603
- C7: renamed from REF**; value NPTH -> 47p; footprint NPTH -> everykey:0603
- C9 (x3): renamed from R3; value 10K -> 0u1
- IC2 (x3): renamed from BTN2; value USER -> FT231XQ; footprint everykey:CK-PTS830 -> everykey:QFN-20
- P4 (x3): renamed from USB1; value USB -> FAN; footprint everykey:USB-MICRO-B -> everykey:HEADER-1x03-2.54
- P5: renamed from REF**; value NPTH -> PWR; footprint NPTH -> everykey:HEADER-1x04-2.5-JST-XH
- R10 (x3): renamed from R14; value 10K -> 47K
- R11, R8: renamed from REF**; value NPTH -> 27; footprint NPTH -> everykey:0603
- R17: renamed from REF**; value NPTH -> 220; footprint NPTH -> everykey:0603
- R2: renamed from REF**; value NPTH -> 1K; footprint NPTH -> everykey:0603
- moved P5 150.3 mm to (197.2, 58.0), turned to 270 degrees
- moved R11 95.6 mm to (179.2, 57.0), turned to 270 degrees
- moved C9 75.5 mm to (52.5, 60.0), turned to 180 degrees
- moved C9 73.3 mm to (93.5, 60.0), turned to 180 degrees
- moved C9 71.3 mm to (134.5, 60.0), turned to 180 degrees
- moved R17 70.9 mm to (192.1, 60.9), turned to 180 degrees
- moved C5 64.0 mm to (56.7, 113.1), turned to 180 degrees
- moved C7 63.7 mm to (180.7, 57.0), turned to 270 degrees
- moved C5 62.1 mm to (97.7, 113.1), turned to 180 degrees
- moved P4 60.6 mm to (80.2, 110.4)
- moved C5 60.2 mm to (138.7, 113.1), turned to 180 degrees
- moved P4 60.0 mm to (121.2, 110.4)
- moved P4 59.5 mm to (162.2, 110.4)
- moved IC2 45.6 mm to (57.0, 62.5)
- moved R10 44.9 mm to (80.4, 90.8), turned to 180 degrees
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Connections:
- C13 pad 1: Board_4-Net-(C8-Pad1) -> Board_3-3V3
- C13 pad 2: Board_4-Net-(IC2-Pad8) -> Board_3-GND
- C13 pad 1: Board_3-Net-(C8-Pad1) -> Board_2-3V3
- C13 pad 2: Board_3-Net-(IC2-Pad8) -> Board_2-GND
- C13 pad 1: Board_2-Net-(C8-Pad1) -> Board_1-3V3
- C13 pad 2: Board_2-Net-(IC2-Pad8) -> Board_1-GND
- C5 pad 1: Board_4-/~DTR -> Board_3-3V3
- C5 pad 1: Board_3-/~DTR -> Board_2-3V3
- C5 pad 1: Board_2-/~DTR -> Board_1-3V3
- C9 pad 1: Board_4-FAN_PWM -> Board_3-/FT231_3V3
- C9 pad 2: Board_4-GND -> Board_3-GND
- C9 pad 1: Board_3-FAN_PWM -> Board_2-/FT231_3V3
- C9 pad 2: Board_3-GND -> Board_2-GND
- C9 pad 1: Board_2-FAN_PWM -> Board_1-/FT231_3V3
- C9 pad 2: Board_2-GND -> Board_1-GND
- IC2 pad 1: Board_4-BOOTMODE -> Board_3-TXD
- IC2 pad 2: Board_4-GND -> (no net)
- IC2 pad 1: Board_3-BOOTMODE -> Board_2-TXD
- IC2 pad 2: Board_3-GND -> (no net)
- IC2 pad 1: Board_2-BOOTMODE -> Board_1-TXD
- IC2 pad 2: Board_2-GND -> (no net)
- P4 pad 1: Board_4-Net-(C6-Pad1) -> Board_3-GND
- P4 pad 2: Board_4-Net-(C7-Pad1) -> Board_3-Net-(D1-PadK)
- P4 pad 3: Board_4-Net-(C8-Pad1) -> Board_3-Net-(P4-Pad3)
- P4 pad 1: Board_3-Net-(C6-Pad1) -> Board_2-GND
- P4 pad 2: Board_3-Net-(C7-Pad1) -> Board_2-Net-(D1-PadK)
- P4 pad 3: Board_3-Net-(C8-Pad1) -> Board_2-Net-(P4-Pad3)
- P4 pad 1: Board_2-Net-(C6-Pad1) -> Board_1-GND
- P4 pad 2: Board_2-Net-(C7-Pad1) -> Board_1-Net-(D1-PadK)
- P4 pad 3: Board_2-Net-(C8-Pad1) -> Board_1-Net-(P4-Pad3)
- R10 pad 1: Board_4-/~DTR -> Board_3-SENS2_IN
- R10 pad 2: Board_4-Net-(R14-Pad2) -> Board_3-GND
- R10 pad 1: Board_3-/~DTR -> Board_2-SENS2_IN
- R10 pad 2: Board_3-Net-(R14-Pad2) -> Board_2-GND
- R10 pad 1: Board_2-/~DTR -> Board_1-SENS2_IN
- R10 pad 2: Board_2-Net-(R14-Pad2) -> Board_1-GND
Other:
- board size 175 x 96 mm -> 190 x 102 mm
- board text added: "https://github.com/OpenAirCgn/openairnode-hw/tree/v1.4"
- board text removed: "https://github.com/OpenAirCgn/openairnode-hw/tree/cgn-noise-i2s"
